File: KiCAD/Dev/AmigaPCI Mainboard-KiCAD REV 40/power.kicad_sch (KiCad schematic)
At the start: 79 parts, among them CN205 POW SW, CN206 RESET, CN600 Conn_01x03_Pin, CN601 ATX-24, J10 _RESET, J11 _REGEN, J2 CLK7, J210 Case Fan, U201 74AHC1G09, U206 MIC1232, U215 74HCT03, U219 74AHCT04, U220 74LVC08, U222 74HCT4066, U229 74CBT16233, U303 74HCT74, U600 STM8S001J3M, U601 AP2114H-1.2

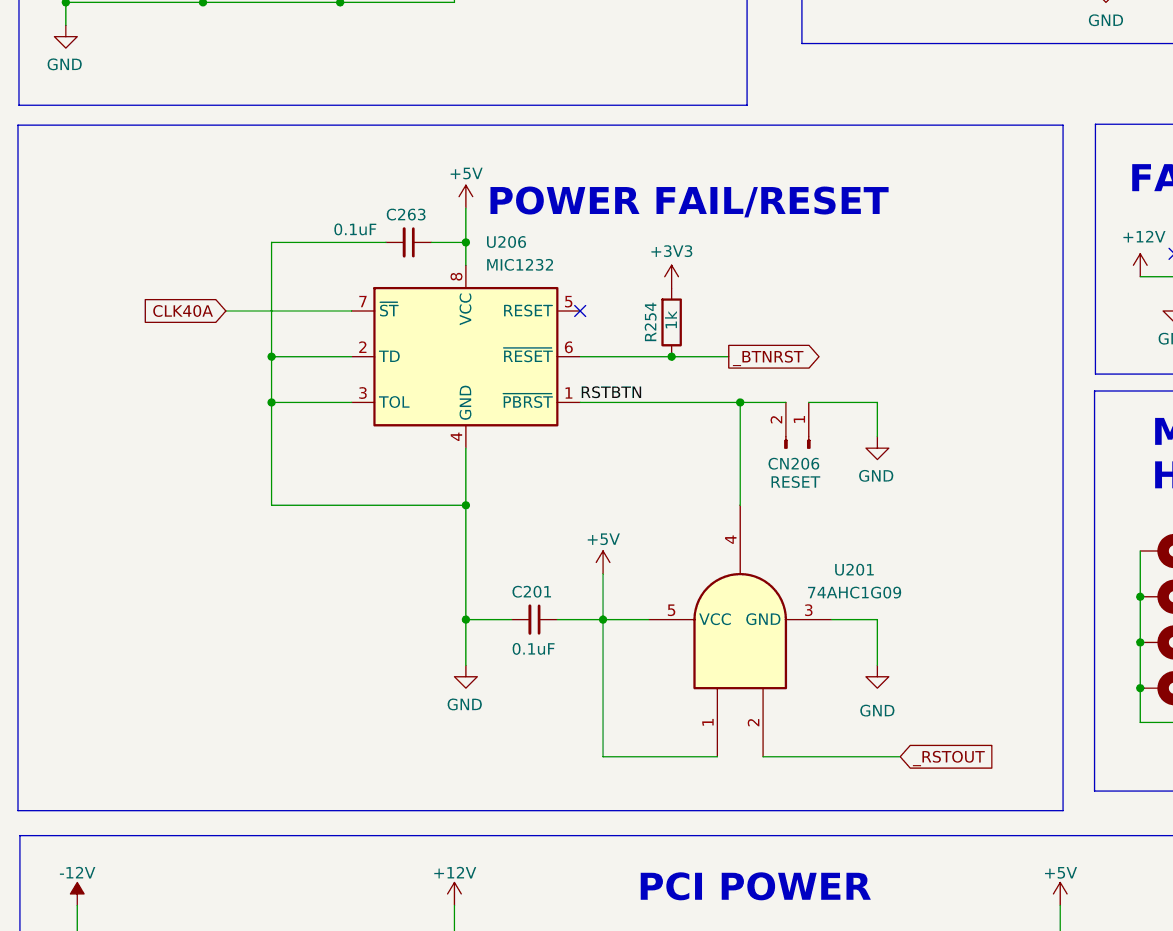
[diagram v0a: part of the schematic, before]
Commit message: Schematic Changes to Clocks 09-JUL-2024
Make changes to support clock generation on CPU local bus card.
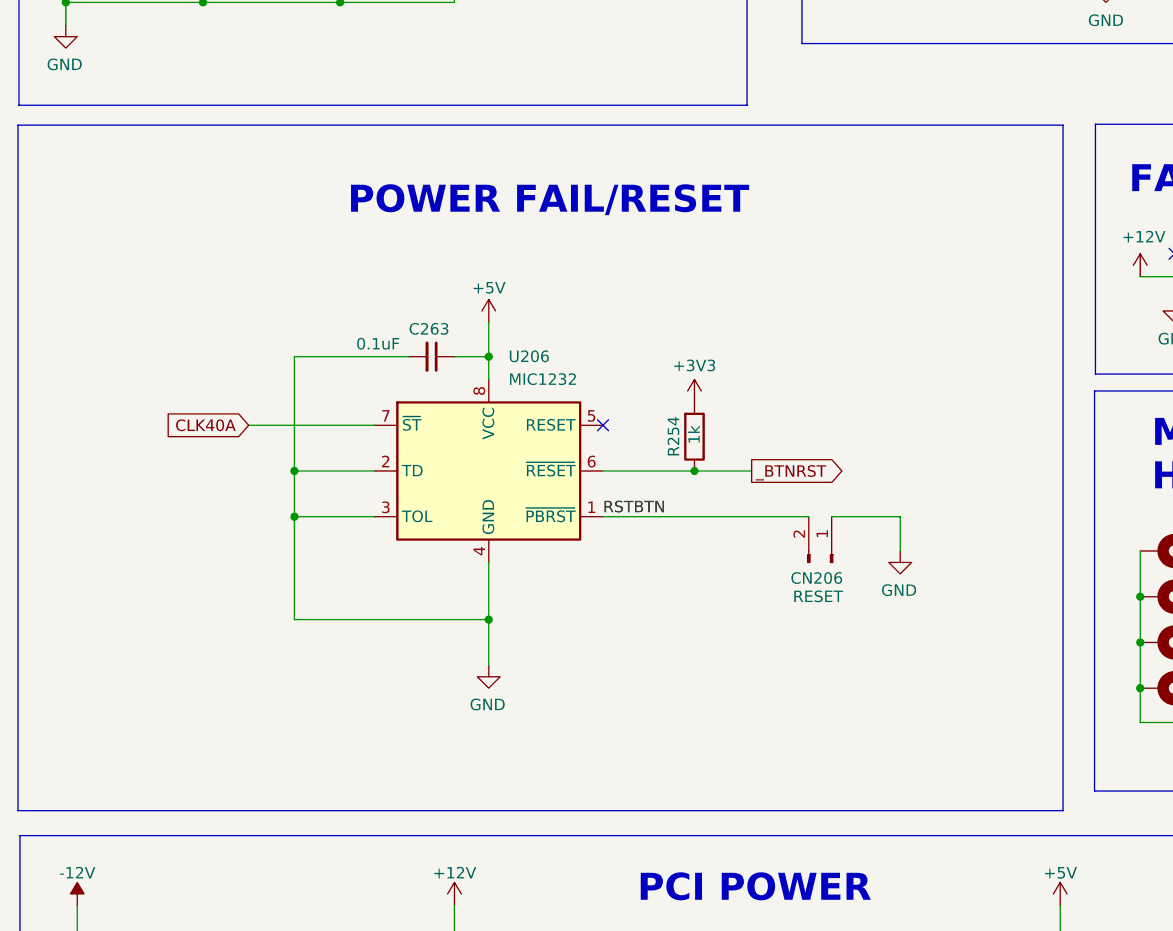
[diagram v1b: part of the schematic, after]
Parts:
- removed C201: 0.1uF, Capacitor_SMD:C_0603_1608Metric, symbol Device:C_Small
- removed U201: 74AHC1G09, Package_TO_SOT_SMD:SOT-23-5, symbol 74xGxx:74AHC1G08
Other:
- moved on the sheet: C263, CN206, R254, U206

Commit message: AmigaPCI Rev 4.0 Schematic Updates 17-JUL-2024
Changed reset circuit, added _DSACKx, Dropped _LOCKE from Local Bus Port,  added CPU Reset In to Local Bus Port.
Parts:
- added C200, C201: 0.1uF, Capacitor_SMD:C_0603_1608Metric, symbol Device:C_Small
- added U231: 74LVC08, Package_SO:TSSOP-14_4.4x5mm_P0.65mm, symbol 74xx:74LS08
- added U232: 74AHC1G09, Package_TO_SOT_SMD:SOT-23-5, symbol 74xGxx:74AHC1G08
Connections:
- net _RESET is gone; now on net _RESETA: J10.1 (Pin_1)
- net +3V3: now also C200.1, C201.1, U231.14 (VCC), U231.2, U232.1, U232.5 (VCC)
- net GND: now also C200.2, C201.2, U231.10, U231.12, U231.13, U231.7 (GND), U231.9, U232.3 (GND)
- net _BTNRST: no longer U220.2
- net _KBRST: no longer U220.1
- net _RESETA: now also U220.3; no longer U220.6
- net _RESETB: now also U231.6; no longer U220.3
- net RSTBTN: no longer names the net of CN206.2 (Pin_2), U206.1 (~{PBRST})
- net RSTBTN: now also U232.4
- new net: U220.2, U220.6, U231.1, U231.5
- new net _CPURST: U231.3
- new net _RSTBTN: U232.2
- new net _RSTOUT: U220.1, U231.4
- no-connect marks 25 -> 27
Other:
- note removed: "RESET"
- moved on the sheet: C110, C111, C112, C113, C114, C115, C116, C117, C118, C119, C120, C121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

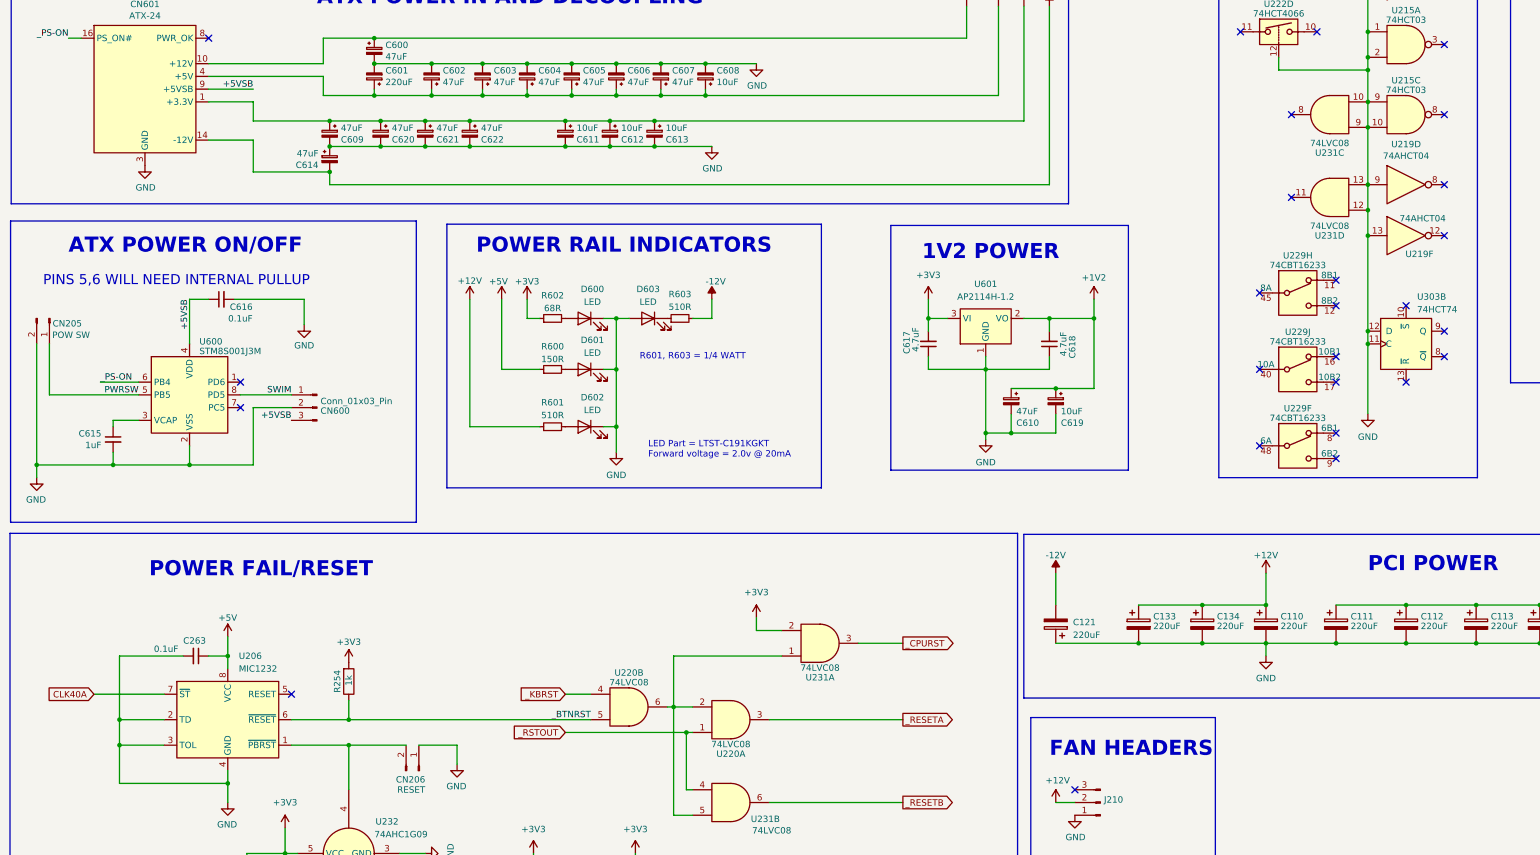
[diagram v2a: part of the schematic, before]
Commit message: AmigaPCI Rev 4.0 Routing
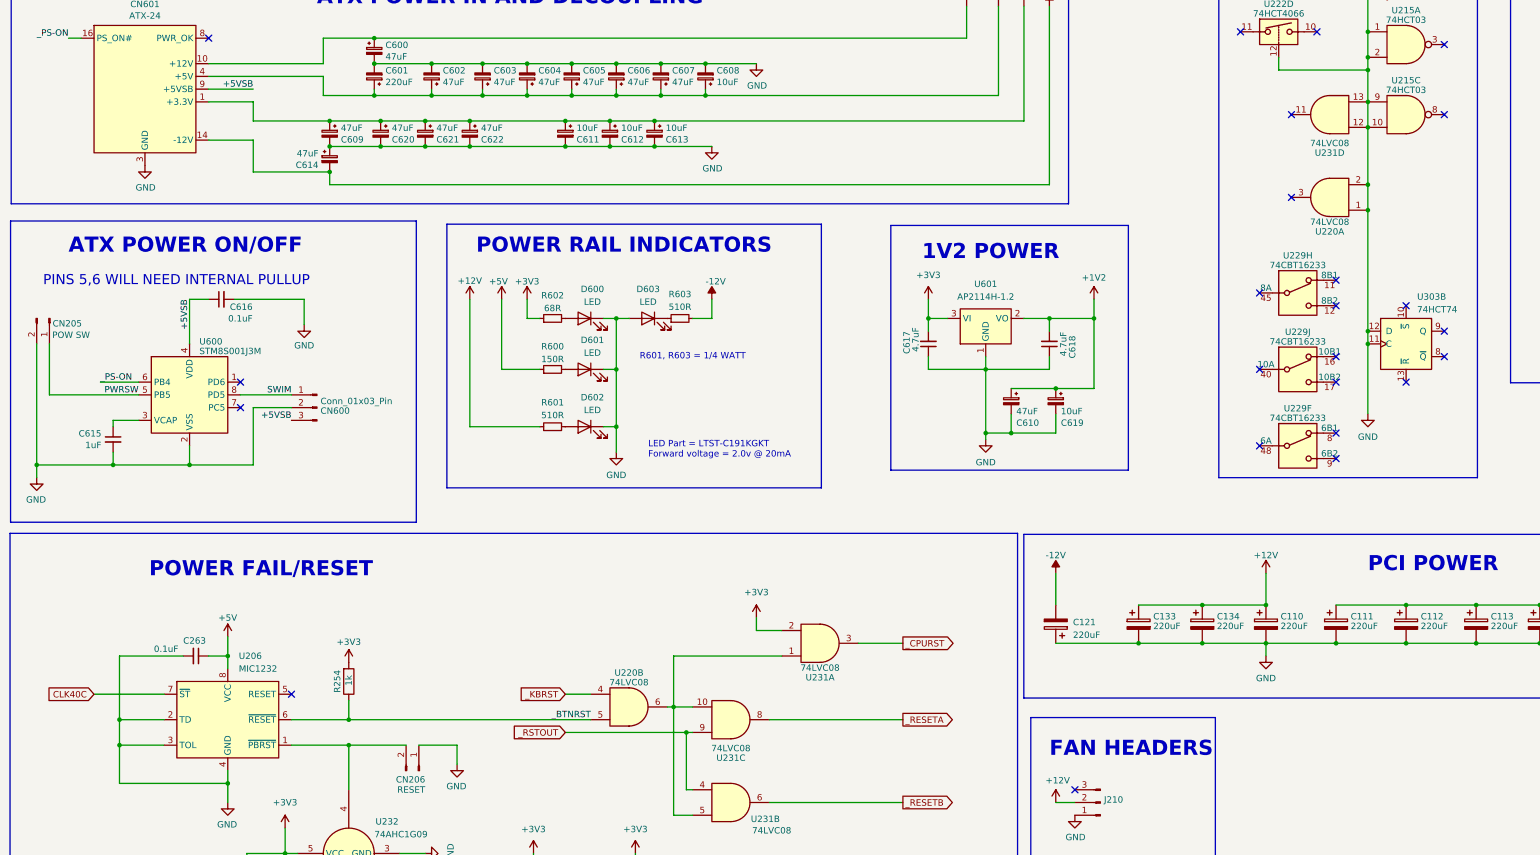
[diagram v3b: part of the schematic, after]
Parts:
- removed unit 6 of U219
- removed unit 4 of U219
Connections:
- net GND: now also U220.1, U220.2; no longer U231.10, U231.9
- net _RESETA: now also U231.8; no longer U220.3
- net _RSTOUT: now also U231.9; no longer U220.1
- net at U220.6, U231.1, U231.5: now also U231.10; no longer U220.2
- net CLK40A renamed CLK40C
- no-connect marks 27 -> 25
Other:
- moved on the sheet: U220A, U231C, U231D
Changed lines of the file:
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@@
 	)
 	(junction
-		(at 290.83 78.74)
-		(diameter 0)
-		(color 0 0 0 0)
-	)
-	(junction
 		(at 290.83 100.33)
 		(diameter 0)
@@
 	)
 	(no_connect
-		(at 306.07 78.74)
-	)
-	(no_connect
 		(at 306.07 54.61)
 	)
@@
 	)
 	(no_connect
-		(at 306.07 68.58)
-	)
-	(no_connect
 		(at 265.43 38.1)
 	)
@@
 	(wire
 		(pts
-			(xy 290.83 73.66) (xy 290.83 78.74)
-		)
-		(stroke
-			(width 0)
-			(type default)
-		)
-	)
-	(wire
-		(pts
 			(xy 114.3 49.53) (xy 114.3 50.8)
 		)
@@
 	(wire
 		(pts
-			(xy 290.83 78.74) (xy 290.83 97.79)
+			(xy 290.83 73.66) (xy 290.83 97.79)
 		)
 		(stroke
@@
 		)
 	)
-	(global_label "CLK40A"
+	(global_label "CLK40C"
 		(shape input)
 		(at 36.83 170.18 180)
@@
 		)
 		(property "Intersheetrefs" "${INTERSHEET_REFS}"
-			(at 26.7691 170.18 0)
+			(at 26.5877 170.18 0)
 			(effects
 				(font
@@
 	(symbol
 		(lib_id "74xx:74LS08")
-		(at 283.21 54.61 180)
+		(at 163.83 175.26 0)
+		(mirror x)
 		(unit 3)
 		(exclude_from_sim no)
@@
 		(dnp no)
 		(property "Reference" "U231"
-			(at 283.21 62.23 0)
+			(at 163.83 182.88 0)
 			(effects
 				(font
@@
 		)
 		(property "Value" "74LVC08"
-			(at 283.21 60.309 0)
+			(at 163.83 180.959 0)
 			(effects
 				(font
@@
 		)
 		(property "Footprint" "Package_SO:TSSOP-14_4.4x5mm_P0.65mm"
-			(at 283.21 54.61 0)
+			(at 163.83 175.26 0)
 			(effects
 				(font
@@
 		)
 		(property "Datasheet" "http://www.ti.com/lit/gpn/sn74LS08"
-			(at 283.21 54.61 0)
+			(at 163.83 175.26 0)
 			(effects
 				(font
@@
 		)
 		(property "Description" ""
-			(at 283.21 54.61 0)
+			(at 163.83 175.26 0)
 			(effects
 				(font
@@
 	)
 	(symbol
-		(lib_id "74xx:74LS04")
-		(at 298.45 78.74 0)
-		(unit 6)
-		(exclude_from_sim no)
-		(in_bom yes)
-		(on_board yes)
-		(dnp no)
-		(property "Reference" "U219"
-			(at 301.117 82.423 0)
-			(effects
-				(font
-					(size 1.27 1.27)
-				)
-			)
-		)
-		(property "Value" "74AHCT04"
-			(at 301.752 75.311 0)
-			(effects
-				(font
-					(size 1.27 1.27)
-				)
-			)
-		)
-		(property "Footprint" "Package_SO:TSSOP-14_4.4x5mm_P0.65mm"
-			(at 298.45 78.74 0)
-			(effects
-				(font
-					(size 1.27 1.27)
-				)
-				(hide yes)
-			)
-		)
-		(property "Datasheet" "http://www.ti.com/lit/gpn/sn74LS04"
-			(at 298.45 78.74 0)
-			(effects
-				(font
-					(size 1.27 1.27)
-				)
-				(hide yes)
-			)
-		)
-		(property "Description" ""
-			(at 298.45 78.74 0)
-			(effects
-				(font
-					(size 1.27 1.27)
-				)
-				(hide yes)
-			)
-		)
-		(pin "1"
-		)
-		(pin "2"
-		)
-		(pin "3"
-		)
-		(pin "4"
-		)
-		(pin "5"
-		)
-		(pin "6"
-		)
-		(pin "8"
-		)
-		(pin "9"
-		)
-		(pin "10"
-		)
-		(pin "11"
-		)
-		(pin "12"
-		)
-		(pin "13"
-		)
-		(pin "14"
-		)
-		(pin "7"
-		)
-		(instances
-			(project "AmigaPCI Mainboard"
-				(path "/72453515-27fe-4336-91f3-e3c8054f7767/4cb777ef-2899-49f4-b38f-a0c07d84fa7d"
-					(reference "U219")
-					(unit 6)
-				)
-			)
-			(project "2000ATX"
-				(path "/bb595301-1c72-49dc-ac6f-007419f3a7fd/00000000-0000-0000-0000-000060bfac72"
-					(reference "U107")
-					(unit 6)
-				)
-			)
-		)
-	)
-	(symbol
 		(lib_id "Device:C_Polarized")
 		(at 298.45 156.21 0)
@@
 	(symbol
 		(lib_id "74xx:74LS08")
-		(at 163.83 175.26 0)
-		(mirror x)
+		(at 283.21 71.12 180)
 		(unit 1)
 		(exclude_from_sim no)
@@
 		(dnp no)
 		(property "Reference" "U220"
-			(at 163.8217 182.0799 0)
+			(at 283.2183 77.9399 0)
 			(effects
 				(font
@@
 		)
 		(property "Value" "74LVC08"
-			(at 163.8217 180.1589 0)
+			(at 283.2183 76.0189 0)
 			(effects
 				(font
@@
 		)
 		(property "Footprint" "Package_SO:TSSOP-14_4.4x5mm_P0.65mm"
-			(at 163.83 175.26 0)
+			(at 283.21 71.12 0)
 			(effects
 				(font
@@
 		)
 		(property "Datasheet" "http://www.ti.com/lit/gpn/sn74LS08"
-			(at 163.83 175.26 0)
+			(at 283.21 71.12 0)
 			(effects
 				(font
@@
 		)
 		(property "Description" ""
-			(at 163.83 175.26 0)
+			(at 283.21 71.12 0)
 			(effects
 				(font
@@
 	(symbol
 		(lib_id "74xx:74LS08")
-		(at 283.21 71.12 180)
+		(at 283.21 54.61 180)
 		(unit 4)
 		(exclude_from_sim no)
@@
 		(dnp no)
 		(property "Reference" "U231"
-			(at 283.21 78.74 0)
+			(at 283.21 62.23 0)
 			(effects
 				(font
@@
 		)
 		(property "Value" "74LVC08"
-			(at 283.21 76.819 0)
+			(at 283.21 60.309 0)
 			(effects
 				(font
@@
 		)
 		(property "Footprint" "Package_SO:TSSOP-14_4.4x5mm_P0.65mm"
-			(at 283.21 71.12 0)
+			(at 283.21 54.61 0)
 			(effects
 				(font
@@
 		)
 		(property "Datasheet" "http://www.ti.com/lit/gpn/sn74LS08"
-			(at 283.21 71.12 0)
+			(at 283.21 54.61 0)
 			(effects
 				(font
@@
 		)
 		(property "Description" ""
-			(at 283.21 71.12 0)
+			(at 283.21 54.61 0)
 			(effects
 				(font
@@
 				)
 			)
-		)
-	)
-	(symbol
-		(lib_id "74xx:74LS04")
-		(at 298.45 68.58 0)
-		(unit 4)
-		(exclude_from_sim no)
-		(in_bom yes)
-		(on_board yes)
-		(dnp no)
-		(property "Reference" "U219"
-			(at 298.45 60.5282 0)
-			(effects
-				(font
-					(size 1.27 1.27)
-				)
-			)
-		)
-		(property "Value" "74AHCT04"
-			(at 298.45 62.8396 0)
-			(effects
-				(font
-					(size 1.27 1.27)
-				)
-			)
-		)
-		(property "Footprint" "Package_SO:TSSOP-14_4.4x5mm_P0.65mm"
-			(at 298.45 68.58 0)
-			(effects
-				(font
-					(size 1.27 1.27)
-				)
-				(hide yes)
-			)
-		)
-		(property "Datasheet" "http://www.ti.com/lit/gpn/sn74LS04"
-			(at 298.45 68.58 0)
-			(effects
-				(font
-					(size 1.27 1.27)
-				)
-				(hide yes)
-			)
-		)
-		(property "Description" ""
-			(at 298.45 68.58 0)
-			(effects
-				(font
-					(size 1.27 1.27)
-				)
-				(hide yes)
-			)
-		)
-		(pin "1"
-		)
-		(pin "2"
-		)
-		(pin "3"
-		)
-		(pin "4"
-		)
-		(pin "5"
-		)
-		(pin "6"
-		)
-		(pin "8"
-		)
-		(pin "9"
-		)
-		(pin "10"
-		)
-		(pin "11"
-		)
-		(pin "12"
-		)
-		(pin "13"
-		)
-		(pin "14"
-		)
-		(pin "7"
-		)
-		(instances
-			(project "AmigaPCI Mainboard"
-				(path "/72453515-27fe-4336-91f3-e3c8054f7767/4cb777ef-2899-49f4-b38f-a0c07d84fa7d"
-					(reference "U219")
-					(unit 4)
-				)
-			)
-			(project "2000ATX"
-				(path "/bb595301-1c72-49dc-ac6f-007419f3a7fd/00000000-0000-0000-0000-000060bfac72"
-					(reference "U107")
-					(unit 4)
-				)
-			)

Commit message: AmigaPCI Mainboard REV 4.0 Routing
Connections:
- net CLK7 renamed LVCLK7
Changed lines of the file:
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@@
 	(title_block
 		(title "AMIGA PCI")
-		(date "2024-07-17")
+		(date "2024-07-31")
 		(rev "4.0")
 	)
@@
 		)
 	)
-	(global_label "CLK7"
+	(global_label "LVCLK7"
 		(shape input)
 		(at 332.74 52.07 0)
@@
 		)
 		(property "Intersheetrefs" "${INTERSHEET_REFS}"
-			(at 340.5028 52.07 0)
+			(at 342.6195 52.07 0)
 			(effects
 				(font
